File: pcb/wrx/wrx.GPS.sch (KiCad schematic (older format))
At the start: 28 parts, among them J3 SMA, J4 DNL U.FL, U101 SE4150L, U104 LP5907 3.3V 250mA, X101 16.368 MHz

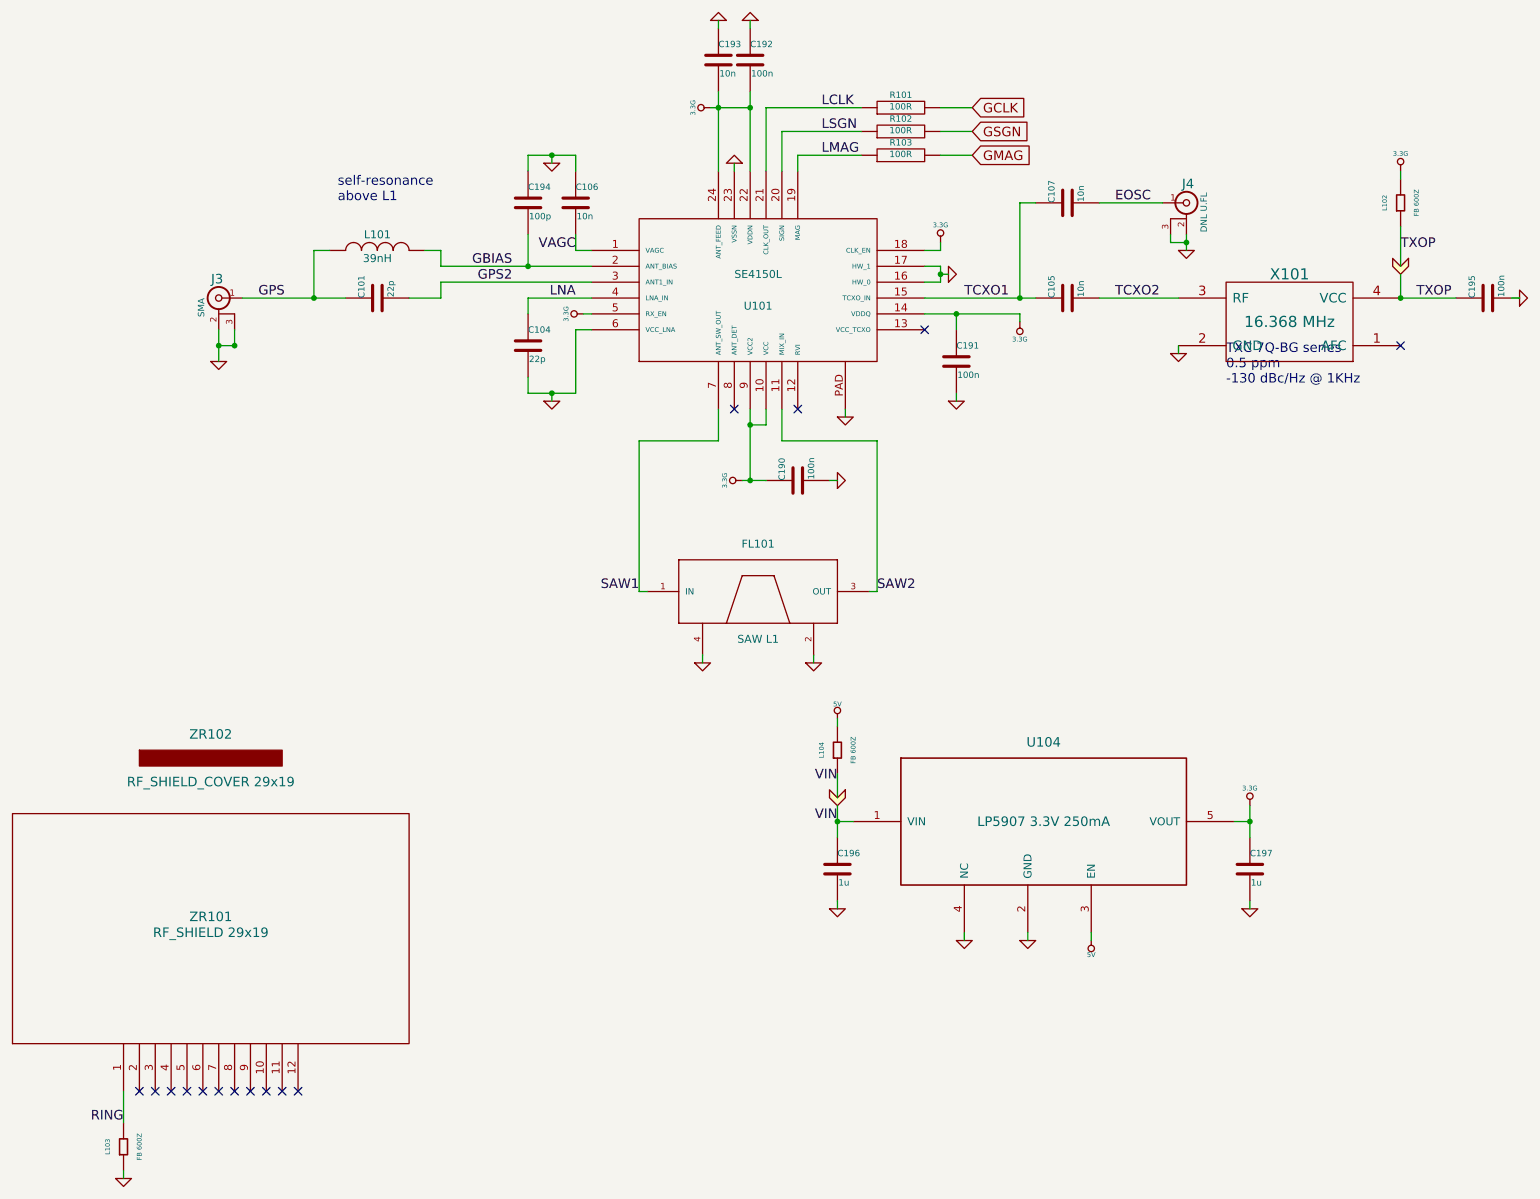
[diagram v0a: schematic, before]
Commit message: big update to, and reorg of, PCB design files
The active antenna PCB has been split-out from the Beagle cape KiCAD
files. This was done so separate BOMs could be more easily created.
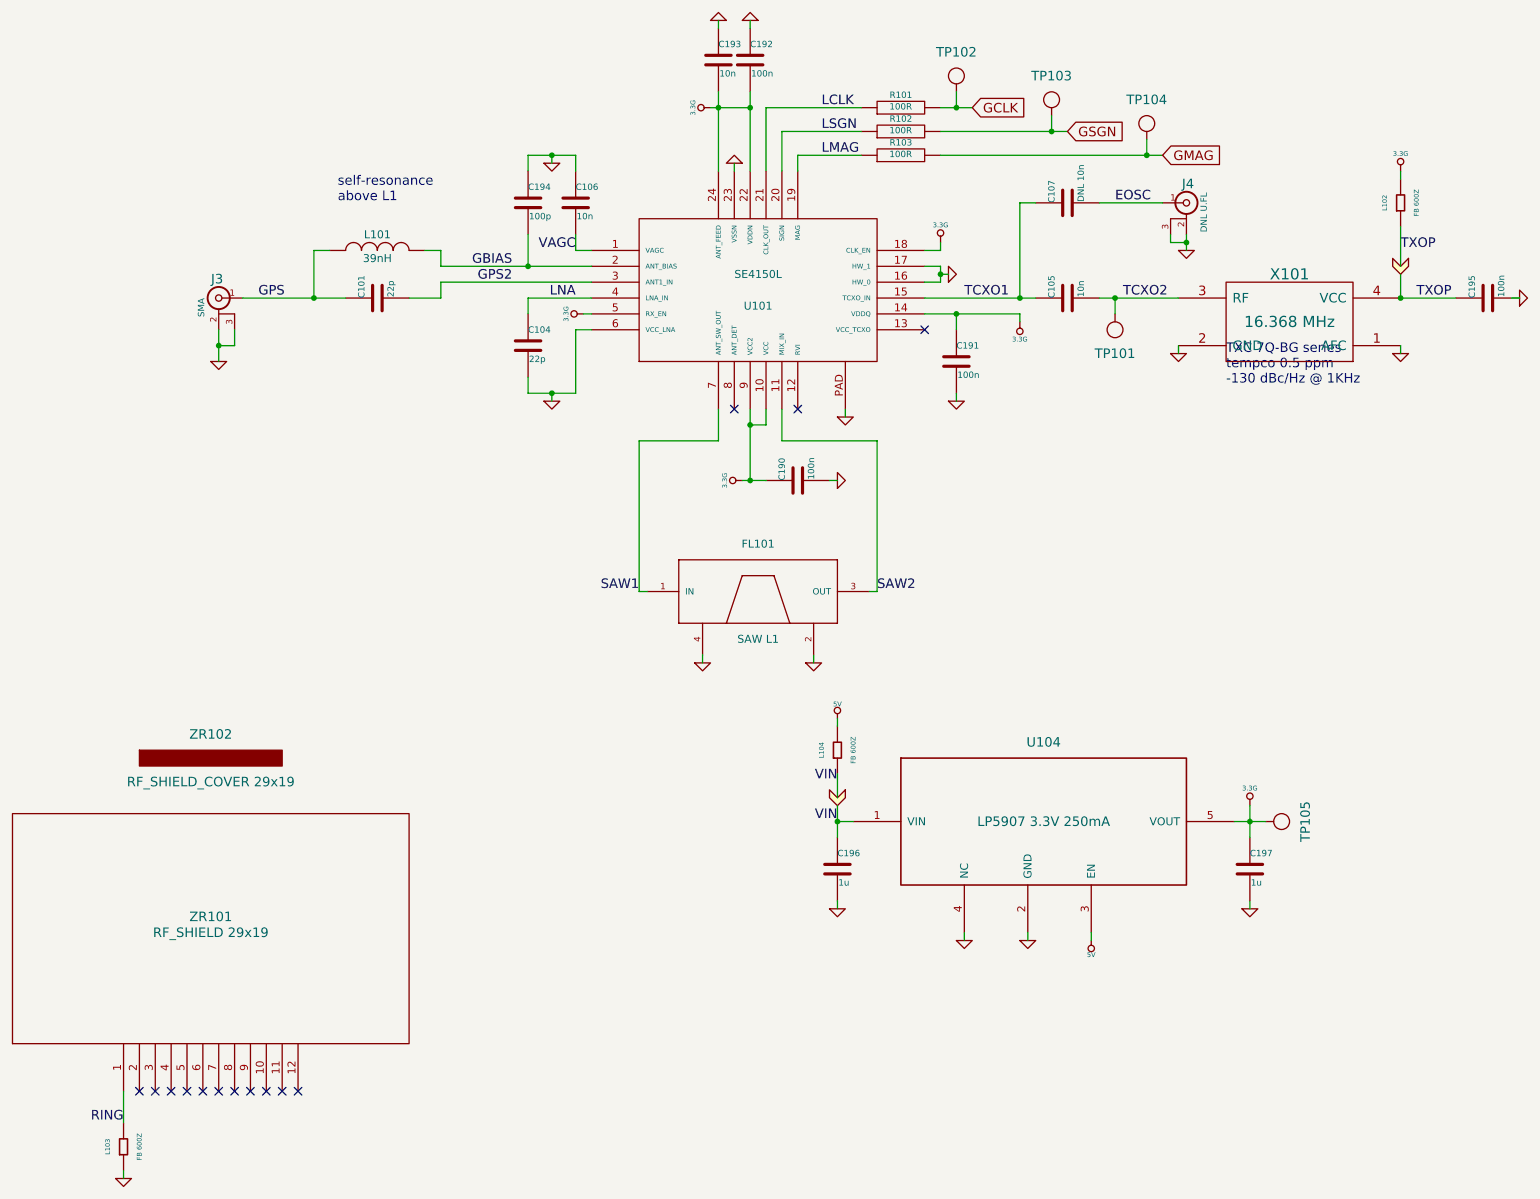
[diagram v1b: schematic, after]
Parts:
- added TP101, TP105: TEST_POINT, wrx-TP_600, symbol TEST_POINT
- added TP102, TP103, TP104: TEST_POINT, wrx-TP_VIA_1250, symbol TEST_POINT
- C107: value 10n -> DNL 10n
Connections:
- net 3.3G: now also TP105.1
- net GCLK: now also TP102.1
- net GMAG: now also TP104.1
- net GND: now also X101.1 (AFC)
- net GSGN: now also TP103.1
- net TCXO2: now also TP101.1
- no-connect marks 15 -> 14
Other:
- note added: "TXC 7Q-BG series\ntempco 0.5 ppm\n-130 dBc/Hz @ 1KHz"
- note removed: "TXC 7Q-BG series\n0.5 ppm\n-130 dBc/Hz @ 1KHz"
